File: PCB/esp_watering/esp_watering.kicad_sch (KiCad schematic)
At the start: 31 parts, among them J1 Zone 0, J10 Zone 9, J11 Zone 10, J12 Zone 11, J13 Zone 12, J14 Zone 13, J15 Zone 14, J16 Zone 15, J17 Zone 16, J18 Zone 17, J19 Zone 18, J2 Zone 1, J20 Zone 19, J21 Flow_Sensor, J22 Power_In, J3 Zone 2, J4 Zone 3, J5 Zone 4, J6 Zone 5, J7 Zone 6, J8 Zone 7, J9 Zone 8, U1 ESP32-DevKit, U2 SN74HC595_1, U3 SN74HC595_2, U4 SN74HC595_3, U5 ULN2003_1, U6 ULN2003_2, U7 ULN2003_3, U8 SSD1306_128x64, U9 PCF8574

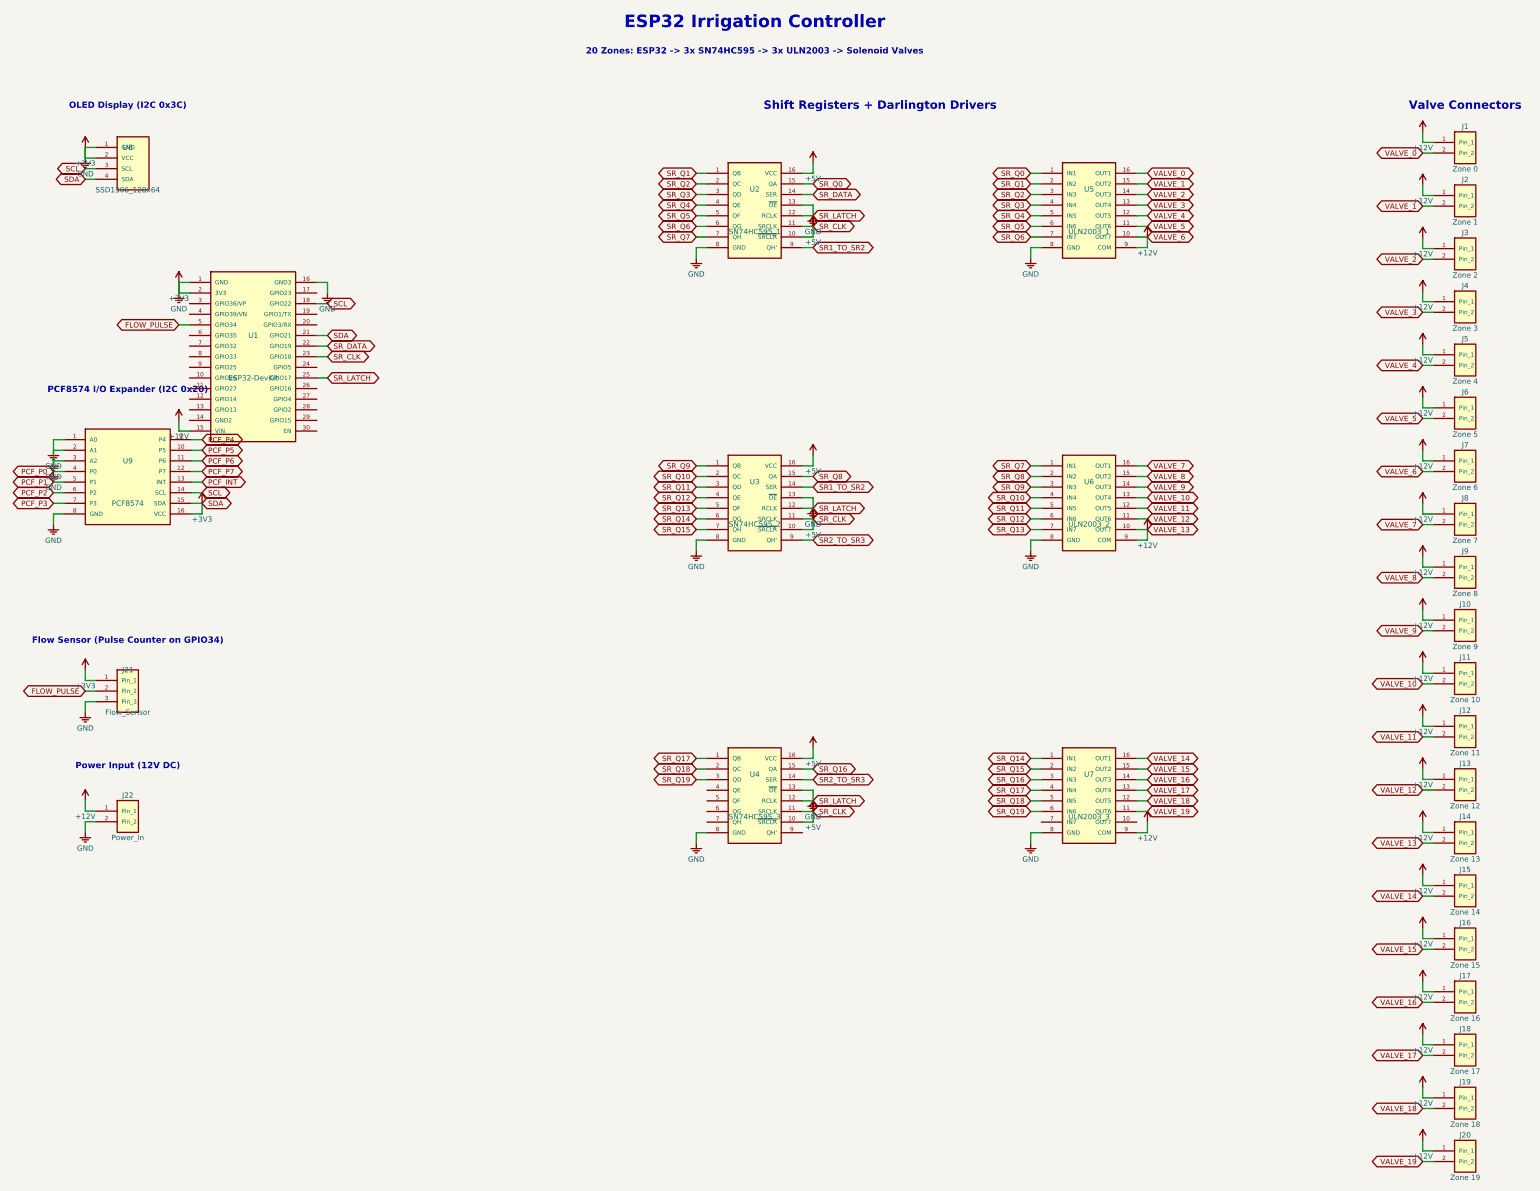
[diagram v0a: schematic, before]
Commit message: Pin reassignment to GPIO12/13/14 and hardware doc refresh
- Shift register pins moved from GPIO19/18/17 to GPIO14/13/12 across
  schematic, generator script, and docs
- Document FS300A flow sensor with passive 1.8k/3.3k divider in place
  of the HW-221 active level shifter (TXS0108E latched against the
  open-collector signal)
- Document the +12V valve / +5V logic / +3V3 (onboard reg) power rails
- Add esphome/zone.yaml package include used by the per-zone refactor
- Note old_version/ as ignored in CLAUDE.md

Co-Authored-By: Claude Opus 4.7 <noreply@anthropic.com>
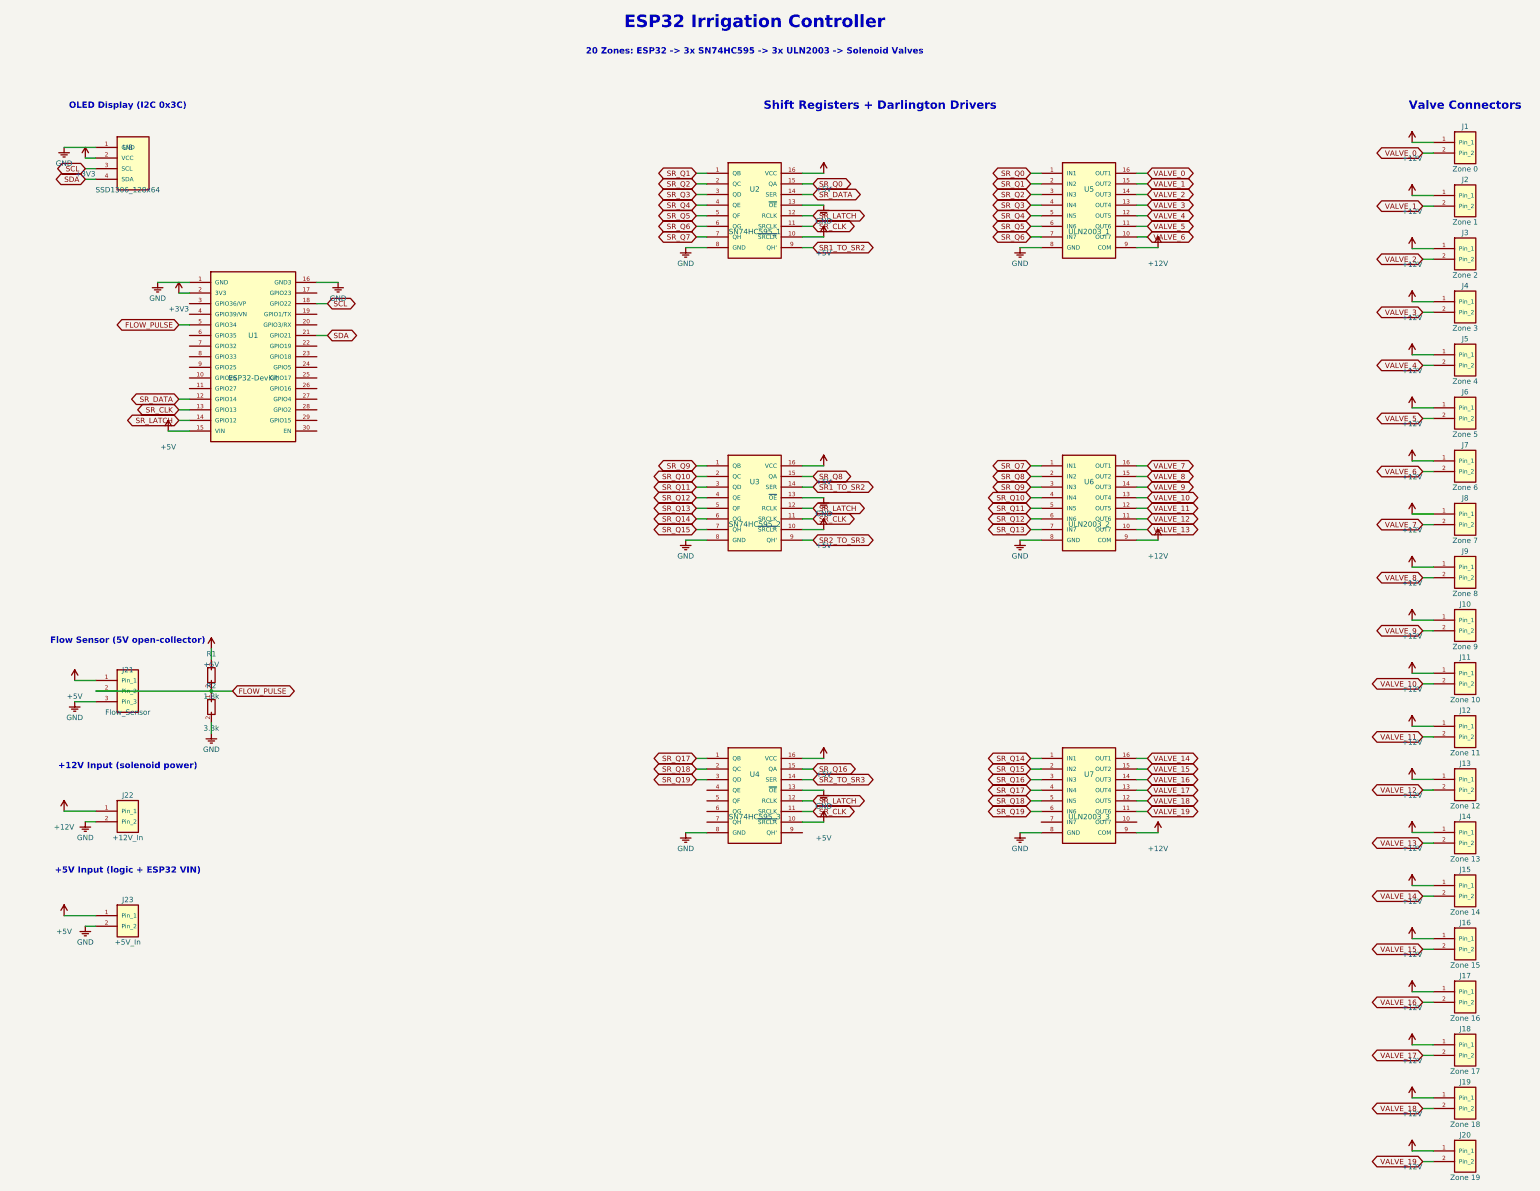
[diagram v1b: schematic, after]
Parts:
- removed U9: PCF8574, symbol irrigation:PCF8574
- added J23: +5V_In, symbol irrigation:Conn_01x02
- added R1: 1.8k, symbol irrigation:R
- added R2: 3.3k, symbol irrigation:R
- J22: value Power_In -> +12V_In
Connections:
- net +12V: no longer J14.2 (Pin_2), J7.2 (Pin_2), U1.15 (VIN), U5.10 (OUT7), U6.10 (OUT7)
- net +3V3: no longer J21.1 (Pin_1), J21.3 (Pin_3), J22.2 (Pin_2), U1.1 (GND), U1.16 (GND3), U1.21 (GPIO21), U1.25 (GPIO17), U2.12 (RCLK), U2.13 (~{OE}), U2.8 (GND), U3.12 (RCLK), U3.13 (~{OE}), U3.8 (GND), U4.12 (RCLK), U4.13 (~{OE}), U4.8 (GND), U5.8 (GND), U6.8 (GND), U7.8 (GND), U8.1 (GND), U8.4 (SDA)
- net +5V: now also J21.1 (Pin_1), U1.15 (VIN), J23.1 (Pin_1), R1.1; no longer U1.23 (GPIO18), U2.11 (SRCLK), U3.11 (SRCLK), U4.11 (SRCLK)
- net FLOW_PULSE: now also R1.2, R2.1
- net SR_DATA: now also U1.12 (GPIO14); no longer U1.22 (GPIO19)
- net SR_CLK: now reaches U1.13 (GPIO13)
- net SR_CLK: now also U2.11 (SRCLK), U3.11 (SRCLK), U4.11 (SRCLK)
- net SR_LATCH: now reaches U1.14 (GPIO12)
- net SR_LATCH: now also U2.12 (RCLK), U3.12 (RCLK), U4.12 (RCLK)
- new net GND: J21.3 (Pin_3), J22.2 (Pin_2), J23.2 (Pin_2), R2.2, U1.1 (GND), U1.16 (GND3), U2.13 (~{OE}), U2.8 (GND), U3.13 (~{OE}), U3.8 (GND), U4.13 (~{OE}), U4.8 (GND), U5.8 (GND), U6.8 (GND), U7.8 (GND), U8.1 (GND)
- new net SDA: U1.21 (GPIO21), U8.4 (SDA)
- new net VALVE_13: J14.2 (Pin_2), U6.10 (OUT7)
- new net VALVE_6: J7.2 (Pin_2), U5.10 (OUT7)
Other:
- note added: "+12V Input (solenoid power)"
- note added: "+5V Input (logic + ESP32 VIN)"
- note added: "Flow Sensor (5V open-collector)"
- note removed: "Flow Sensor (Pulse Counter on GPIO34)"
- note removed: "PCF8574 I/O Expander (I2C 0x20)"
- note removed: "Power Input (12V DC)"
